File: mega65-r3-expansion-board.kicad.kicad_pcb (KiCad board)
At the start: 4 copper layers, 215 x 126.9 mm, 115 parts, among them J1 Conn_01x04, J10 PMOD2, J11 Conn_02x05_Odd_Even, J12 Conn_02x17_Odd_Even, J13 Conn_02x17_Odd_Even, J14 Component A/V, J15 ESP32 Connector, J16 MD-90SM, J17 Conn_01x03, J18 Conn_01x02, J19 Conn_01x03, J2 Conn_01x04, J20 Conn_01x02, J21 Conn_01x03, J3 C64_User_Port, J4 Conn_01x02, J5 C64_Tape_Port, J6 OKR-T/3-W12-C, J7 Conn_02x06_Odd_Even, J8 Conn_02x06_Odd_Even, J9 PMOD1, U1 74HC595, U10 74LS125, U11 74HC595, U12 74LS125, U13 74LS125, U2 74LVC165, U3 74LS125, U4 74HC595, U5 74LVC165, U6 74HC595, U7 74LVC165, U8 74LS125, U9 74LS125

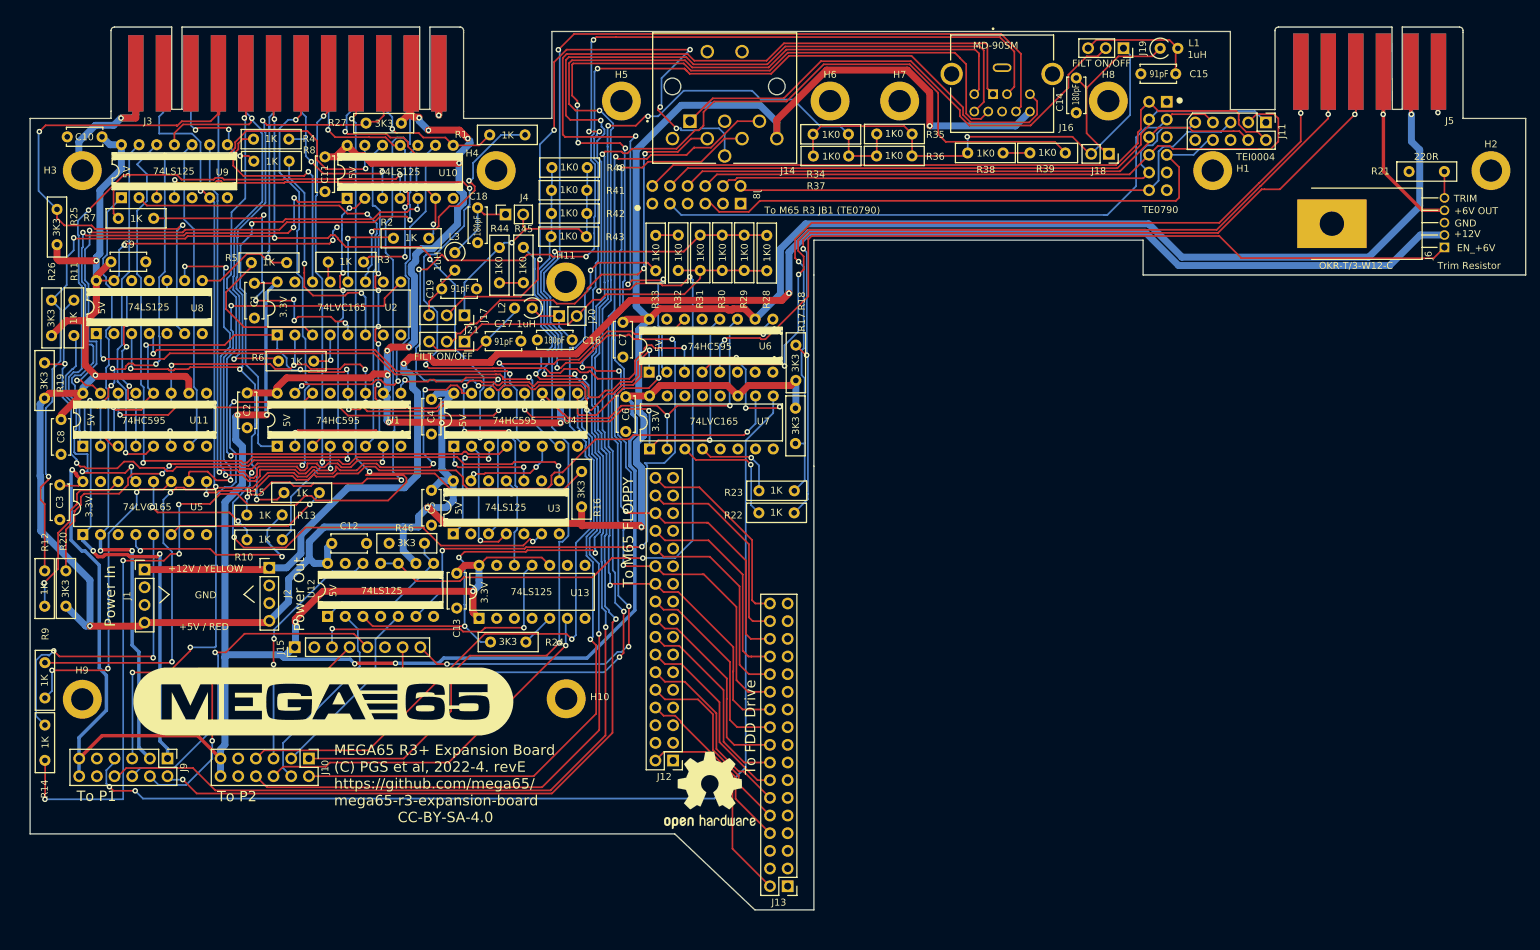
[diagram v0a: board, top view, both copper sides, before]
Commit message: Remove everything not needed for JTAG loader board testing
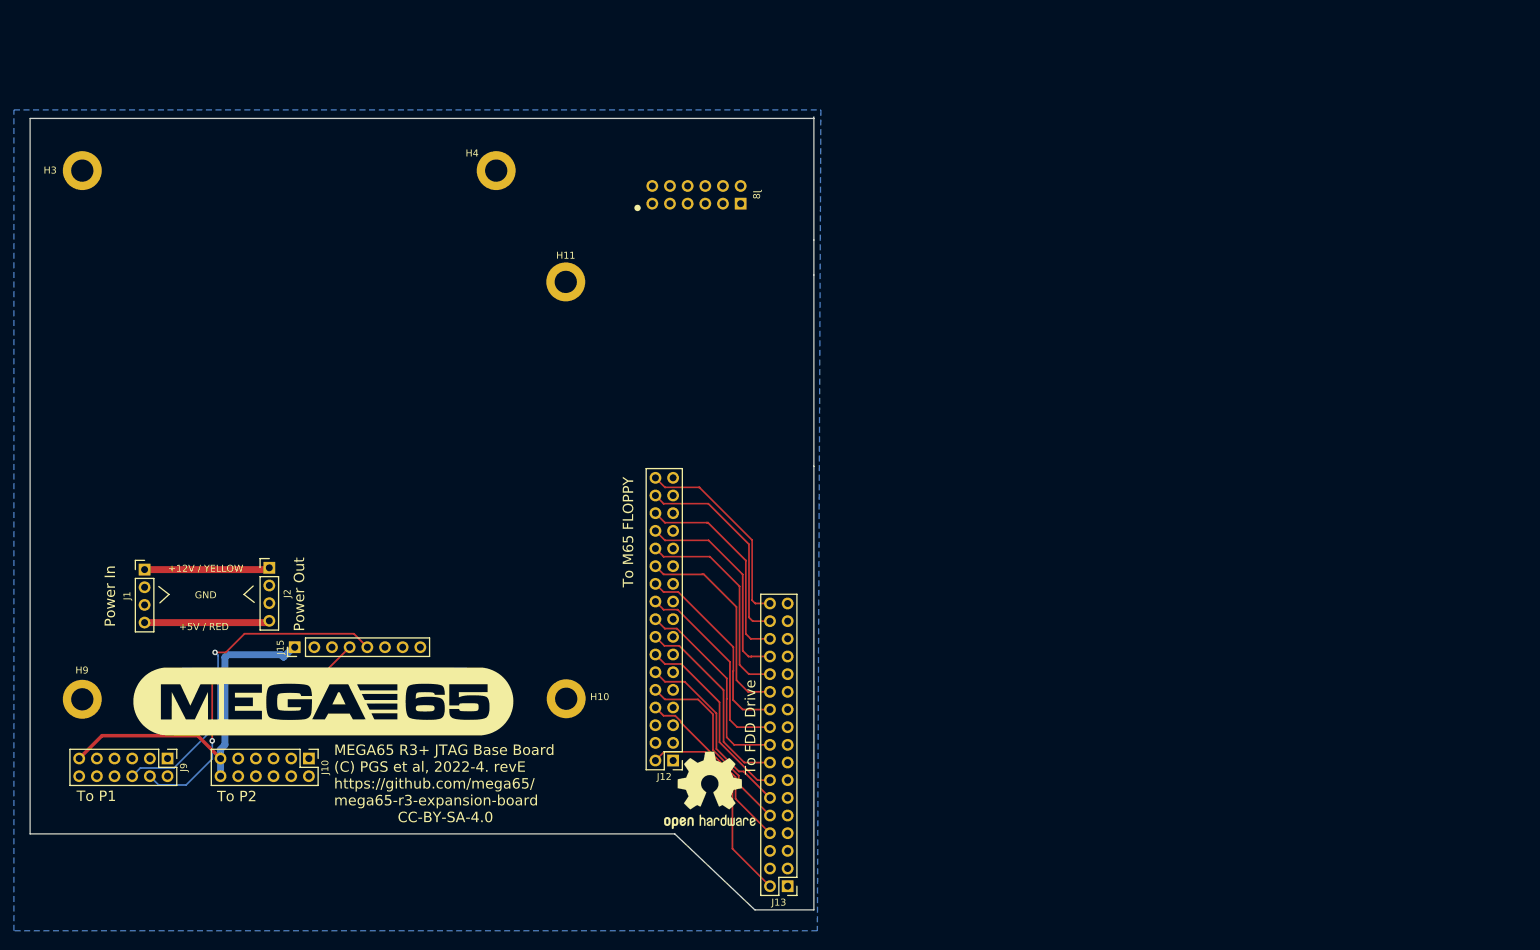
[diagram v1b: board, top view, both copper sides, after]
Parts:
- removed C1, C10, C11, C12, C13, C2, C3, C4, C5, C6, C7, C8, C9: 0.1uF, Capacitor_THT:C_Disc_D5.0mm_W2.5mm_P5.00mm
- removed C14, C16, C18: 180pF, Capacitor_THT:C_Disc_D5.0mm_W2.5mm_P5.00mm
- removed C15, C17, C19: 91pF, Capacitor_THT:C_Disc_D5.0mm_W2.5mm_P5.00mm
- removed H1, H2, H5, H6, H7, H8: MountingHole_Pad, MountingHole:MountingHole_3.2mm_M3_DIN965_Pad
- removed J11: Conn_02x05_Odd_Even, Connector_PinHeader_2.54mm:PinHeader_2x05_P2.54mm_Vertical
- removed J14: Component A/V, snapeda:CUI_SDF-80J
- removed J16: MD-90SM, snapeda:CUI_MD-90SM
- removed J17, J19, J21: Conn_01x03, Connector_PinSocket_2.54mm:PinSocket_1x03_P2.54mm_Vertical
- removed J18, J20, J4: Conn_01x02, Connector_PinSocket_2.54mm:PinSocket_1x02_P2.54mm_Vertical
- removed J3: C64_User_Port, snapeda:C64-User-Port-Male
- removed J5: C64_Tape_Port, HackupNet:C64-Cassette-Port-Male
- removed J6: OKR-T/3-W12-C, snapeda:TO-220-FP-5
- removed J7: Conn_02x06_Odd_Even, Connector_PinHeader_2.54mm:PinHeader_2x06_P2.54mm_Vertical
- removed L1, L2, L3: 1uH, Inductor_THT:L_Axial_L6.6mm_D2.7mm_P2.54mm_Vertical_Vishay_IM-2
- removed R1, R10, R11, R12, R13, R14, R15, R2, R22, R23, R3, R4, R5, R6, R7, R8, R9: 1K, snapeda:Labeled Resistor
- removed R16, R17, R18, R19, R20, R24, R25, R26, R27, R46: 3K3, snapeda:Labeled Resistor
- removed R21: 220R, snapeda:Labeled Resistor
- removed R28, R29, R30, R31, R32, R33, R34, R35, R36, R37, R38, R39, R40, R41, R42, R43, R44, R45: 1K0, snapeda:Labeled Resistor
- removed U1, U11, U4, U6: 74HC595, snapeda:DIP-16_LS_Family
- removed U10, U13, U3, U8, U9: 74LS125, snapeda:DIP-14_74LS06
- removed U12: 74LS125, snapeda:DIP-14_W7.62mm
- removed U2, U5, U7: 74LVC165, snapeda:DIP-16_LVC_Family
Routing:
- net +5V: track 724.8 -> 18.0 mm, vias 20 -> 0
- net +3V3: track 339.3 -> 51.4 mm, vias 7 -> 0
- net /C1565 External C65 Drive Port/SERIO_5V: track 283.0 -> 0.00 mm, vias 11 -> 0
- net COMP_COMP2: track 242.6 -> 0.00 mm, vias 2 -> 0
- net /C1565 External C65 Drive Port/CLOCK_5V: track 217.9 -> 0.00 mm, vias 5 -> 0
- net +12V_FUSED: track 228.7 -> 17.7 mm, vias 2 -> 0
- net 1565_LD_5V: track 210.7 -> 0.00 mm, vias 4 -> 0
- net COMP_COMP5: track 207.9 -> 0.00 mm, vias 4 -> 0
- net /User Port & Tape Port/CNT1: track 204.1 -> 0.00 mm, vias 7 -> 0
- net EXP_LATCH: track 202.1 -> 0.00 mm, vias 10 -> 0
- net EXP_CLOCK: track 186.0 -> 0.00 mm, vias 11 -> 0
- net /User Port & Tape Port/CNT2: track 182.6 -> 0.00 mm, vias 7 -> 0
- net /User Port & Tape Port/SP2: track 175.1 -> 0.00 mm, vias 7 -> 0
- net /User Port & Tape Port/PA2: track 170.5 -> 0.00 mm, vias 6 -> 0
- net /User Port & Tape Port/SP1: track 157.7 -> 0.00 mm, vias 5 -> 0
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- added copper zone on B.Cu, net GND
- removed copper zone on In1.Cu, net GND
- removed copper zone on In2.Cu, net GND
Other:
- board size 215 x 126.9 mm -> 112.7 x 114 mm
- copper layers 4 -> 2
- board text added: "MEGA65 R3+ JTAG Base Board (C) PGS et al, 2022-4. revE https://github.com/mega65/ mega65-r3-expansion-board CC-BY-SA-4.0"
- board text removed: "+12V"
- board text removed: "+6V OUT"
- board text removed: "EN_+6V"
- board text removed: "FILT ON/OFF"
- board text removed: "GND"
- board text removed: "MEGA65 R3+ Expansion Board (C) PGS et al, 2022-4. revE https://github.com/mega65/ mega65-r3-expansion-board CC-BY-SA-4.0"
- board text removed: "TE0790"
- board text removed: "TEI0004"
- board text removed: "TRIM"
- board text removed: "To M65 R3 JB1 (TE0790)"
- board text removed: "Trim Resistor"

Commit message: Minor changes from DRC.
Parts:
- added J14: Conn_02x05_Odd_Even, Connector_PinHeader_2.54mm:PinHeader_2x05_P2.54mm_Vertical, F.Cu at (59.3, 55.8)
- added J7: Conn_02x06_Odd_Even, Connector_PinHeader_2.54mm:PinHeader_2x06_P2.54mm_Vertical, B.Cu at (43.9, 52.5)
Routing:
- net /Multiplexor Interconnect Bus/TE0790_3: track 0.00 -> 119.3 mm
- net /Multiplexor Interconnect Bus/TE0790_7: track 0.00 -> 106.7 mm
- net /Multiplexor Interconnect Bus/TE0790_4: track 0.00 -> 104.5 mm
- net /Multiplexor Interconnect Bus/TE0790_2: track 0.00 -> 101.4 mm
- net /Multiplexor Interconnect Bus/TE0790_6: track 0.00 -> 100.9 mm
- net /Multiplexor Interconnect Bus/TE0790_8: track 0.00 -> 100.2 mm
- net /Multiplexor Interconnect Bus/TE0790_12: track 0.00 -> 91.8 mm
- net /Multiplexor Interconnect Bus/TE0790_10: track 0.00 -> 89.4 mm, vias 0 -> 1
- net +3V3: track 51.4 -> 53.9 mm
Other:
- board size 112.7 x 114 mm -> 112.7 x 113.8 mm

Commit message: Start fixing the jtag connector positioning
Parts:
- J8: moved to F.Cu
- moved J7 13.2 mm to (44.1, 39.2)
- moved J8 12.7 mm to (108.3, 52.5)
- moved J14 12.4 mm to (59.1, 43.4)
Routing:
- net /Multiplexor Interconnect Bus/TE0790_3: track 119.3 -> 0.00 mm
- net /Multiplexor Interconnect Bus/TE0790_7: track 106.7 -> 0.00 mm
- net /Multiplexor Interconnect Bus/TE0790_4: track 104.5 -> 0.00 mm
- net /Multiplexor Interconnect Bus/TE0790_2: track 101.4 -> 0.00 mm
- net /Multiplexor Interconnect Bus/TE0790_6: track 100.9 -> 0.00 mm
- net /Multiplexor Interconnect Bus/TE0790_8: track 100.2 -> 0.00 mm
- net /Multiplexor Interconnect Bus/TE0790_12: track 91.8 -> 0.00 mm
- net /Multiplexor Interconnect Bus/TE0790_10: track 89.4 -> 0.00 mm, vias 1 -> 0
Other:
- board size 112.7 x 113.8 mm -> 112.7 x 128 mm

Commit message: Add in the temodule and the step layers
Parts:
- ?: renamed from J9; footprint Connector_PinHeader_2.54mm:PinHeader_2x06_P2.54mm_Vertical -> Connector_PinSocket_2.54mm:PinSocket_2x06_P2.54mm_Horizontal
- J10: footprint Connector_PinHeader_2.54mm:PinHeader_2x06_P2.54mm_Vertical -> Connector_PinSocket_2.54mm:PinSocket_2x06_P2.54mm_Horizontal
- moved J10 12.8 mm to (46.1, 132.2), turned to 90 degrees
- moved ? 12.7 mm to (25.9, 132.2), turned to 90 degrees
- moved J14 4.08 mm to (55.1, 43.4)
- moved J7 4.08 mm to (40.0, 39.2)
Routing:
- net /Multiplexor Interconnect Bus/TE0790_2: track 0.00 -> 108.0 mm
- net /Multiplexor Interconnect Bus/TE0790_4: track 0.00 -> 103.9 mm, vias 0 -> 1
- net /Multiplexor Interconnect Bus/TE0790_6: track 0.00 -> 99.9 mm, vias 0 -> 1
- net /Multiplexor Interconnect Bus/TE0790_8: track 0.00 -> 94.8 mm, vias 0 -> 1
- net /Multiplexor Interconnect Bus/TE0790_3: track 0.00 -> 90.0 mm, vias 0 -> 1
- net /Multiplexor Interconnect Bus/TE0790_7: track 0.00 -> 87.5 mm, vias 0 -> 1
- net /Multiplexor Interconnect Bus/TE0790_10: track 0.00 -> 85.5 mm, vias 0 -> 1
- net /Multiplexor Interconnect Bus/TE0790_12: track 0.00 -> 84.0 mm, vias 0 -> 1
- added copper zone on F.Cu, net GND
